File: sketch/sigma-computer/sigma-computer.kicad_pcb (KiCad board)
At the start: 2 copper layers, 120 x 80 mm, 4 parts

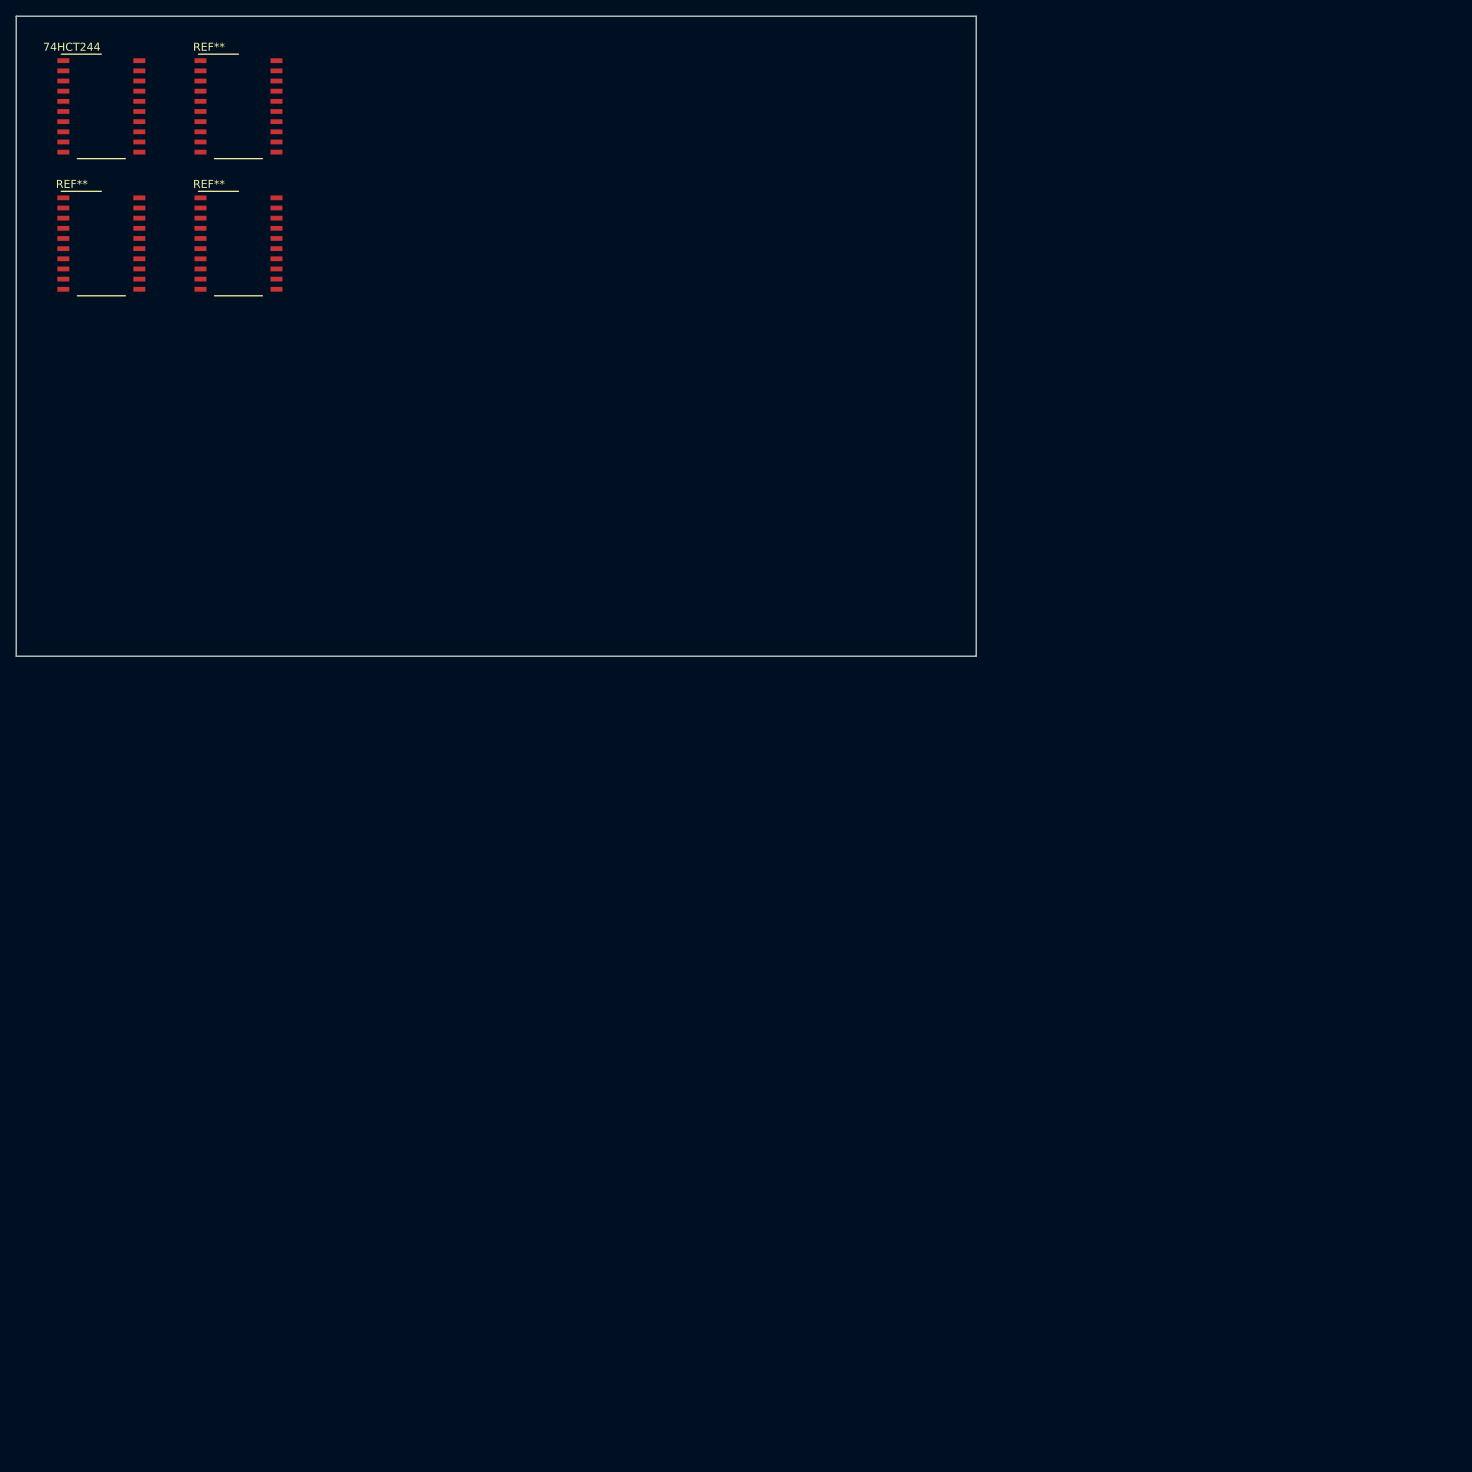
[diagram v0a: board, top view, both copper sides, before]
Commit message: Changed the registers and buffers
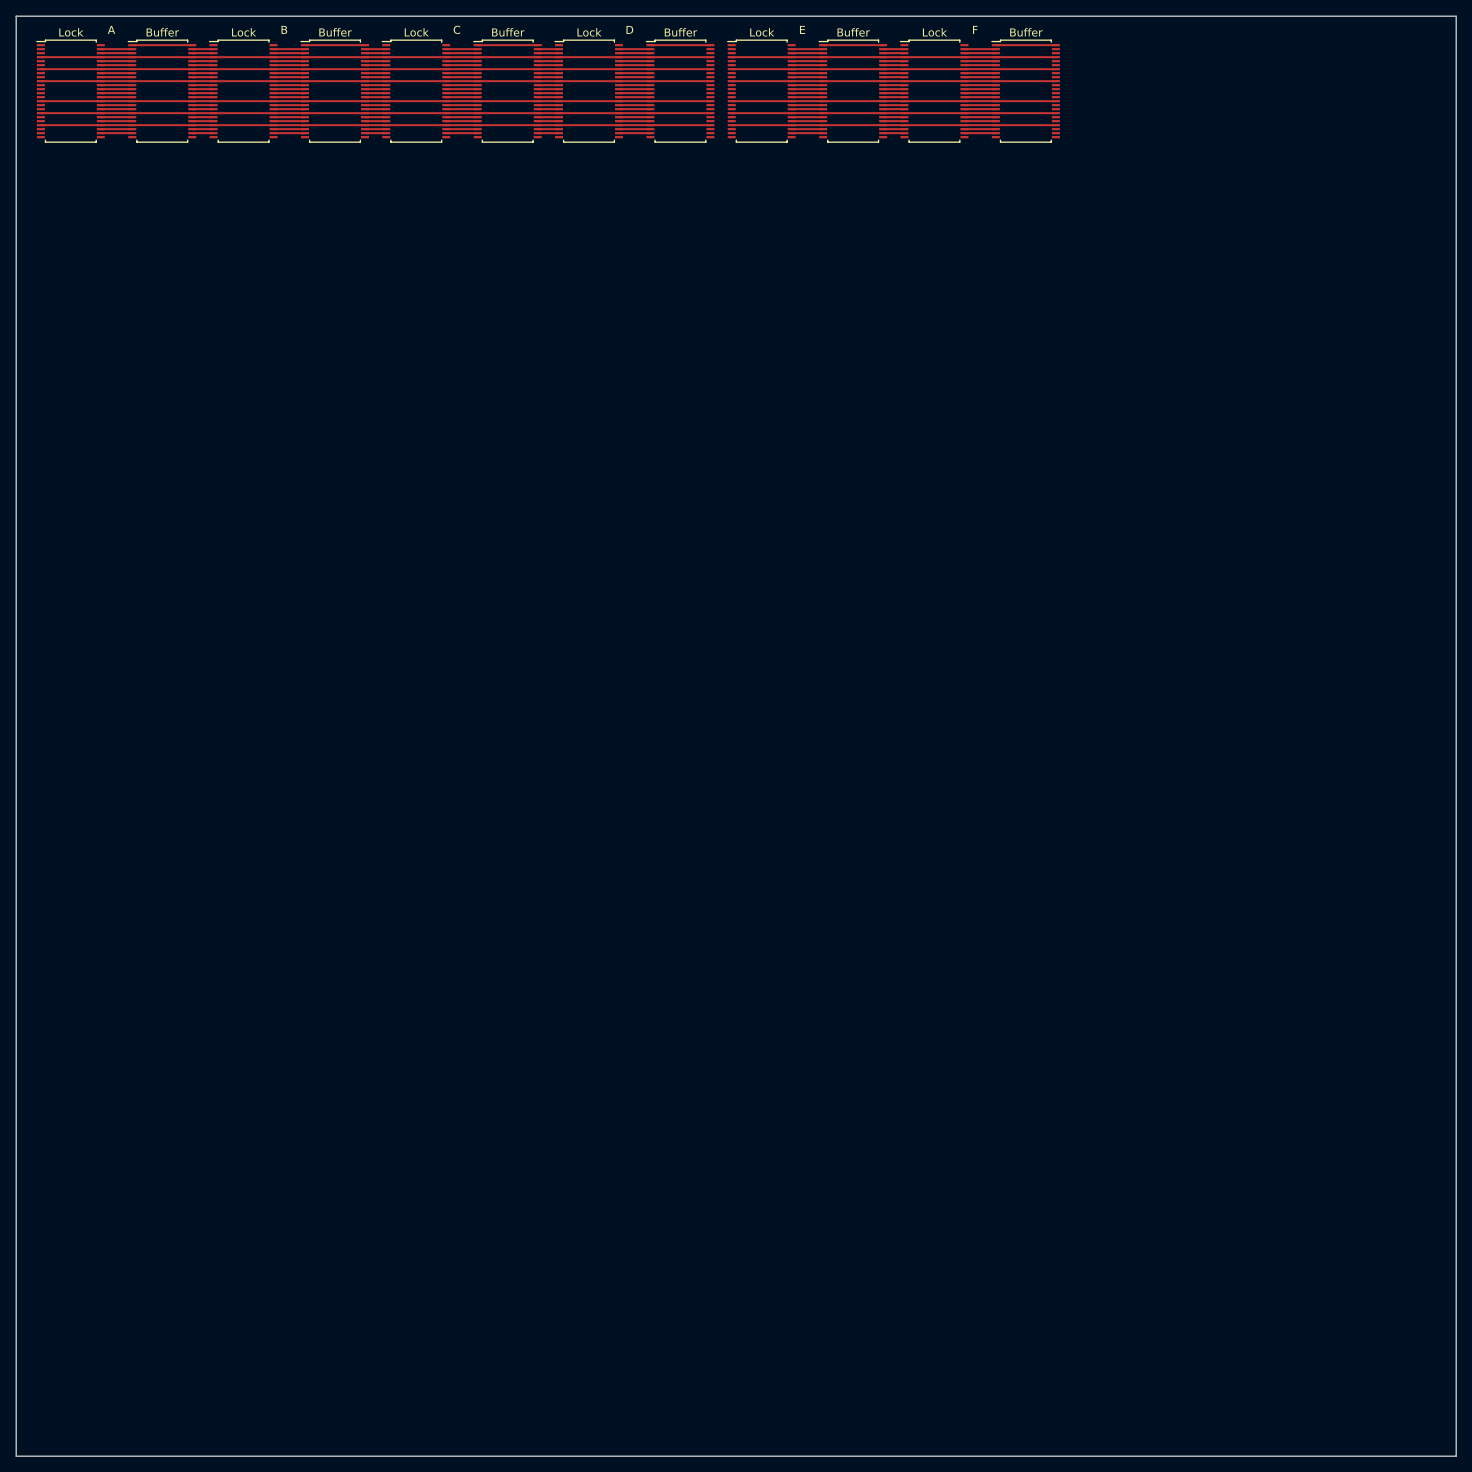
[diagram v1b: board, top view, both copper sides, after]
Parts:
- removed 74HCT244, REF** (x3): SO-20_12.8x7.5mm_P1.27mm, Package_SO:SO-20_12.8x7.5mm_P1.27mm
- added Buffer: , Housings_SSOP:TSSOP-48_6.1x12.5mm_Pitch0.5mm, F.Cu at (134.6, 39.4)
- added Buffer: , Housings_SSOP:TSSOP-48_6.1x12.5mm_Pitch0.5mm, F.Cu at (156.2, 39.4)
- added Buffer: , Housings_SSOP:TSSOP-48_6.1x12.5mm_Pitch0.5mm, F.Cu at (91.4, 39.4)
- added Buffer: , Housings_SSOP:TSSOP-48_6.1x12.5mm_Pitch0.5mm, F.Cu at (113.0, 39.4)
- added Buffer: , Housings_SSOP:TSSOP-48_6.1x12.5mm_Pitch0.5mm, F.Cu at (69.8, 39.4)
- added Buffer: , Housings_SSOP:TSSOP-48_6.1x12.5mm_Pitch0.5mm, F.Cu at (48.3, 39.4)
- added Lock: , Housings_SSOP:TSSOP-48_6.1x12.5mm_Pitch0.5mm, F.Cu at (144.8, 39.4)
- added Lock: , Housings_SSOP:TSSOP-48_6.1x12.5mm_Pitch0.5mm, F.Cu at (123.2, 39.4)
- added Lock: , Housings_SSOP:TSSOP-48_6.1x12.5mm_Pitch0.5mm, F.Cu at (101.6, 39.4)
- added Lock: , Housings_SSOP:TSSOP-48_6.1x12.5mm_Pitch0.5mm, F.Cu at (80.0, 39.4)
- added Lock: , Housings_SSOP:TSSOP-48_6.1x12.5mm_Pitch0.5mm, F.Cu at (58.4, 39.4)
- added Lock: , Housings_SSOP:TSSOP-48_6.1x12.5mm_Pitch0.5mm, F.Cu at (36.8, 39.4)
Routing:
- net (no net): track 0.00 -> 1338.2 mm
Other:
- board size 120 x 80 mm -> 180 x 180 mm
- board text added: "A"
- board text added: "B"
- board text added: "C"
- board text added: "D"
- board text added: "E"
- board text added: "F"

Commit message: Changes in the schematic
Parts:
- removed Buffer (x6), Lock (x6): , Housings_SSOP:TSSOP-48_6.1x12.5mm_Pitch0.5mm
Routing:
- net (no net): track 1338.2 -> 0.00 mm
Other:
- board text removed: "A"
- board text removed: "B"
- board text removed: "C"
- board text removed: "D"
- board text removed: "E"
- board text removed: "F"
